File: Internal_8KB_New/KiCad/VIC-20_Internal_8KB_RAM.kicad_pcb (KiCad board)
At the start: 2 copper layers, 66 x 62.2 mm, 11 parts, among them J1 RAM Decoder, J2 UD4, J3 UE4, U1 74HCT04, U2 74HCT138, U3 62256, U4 74HCT30

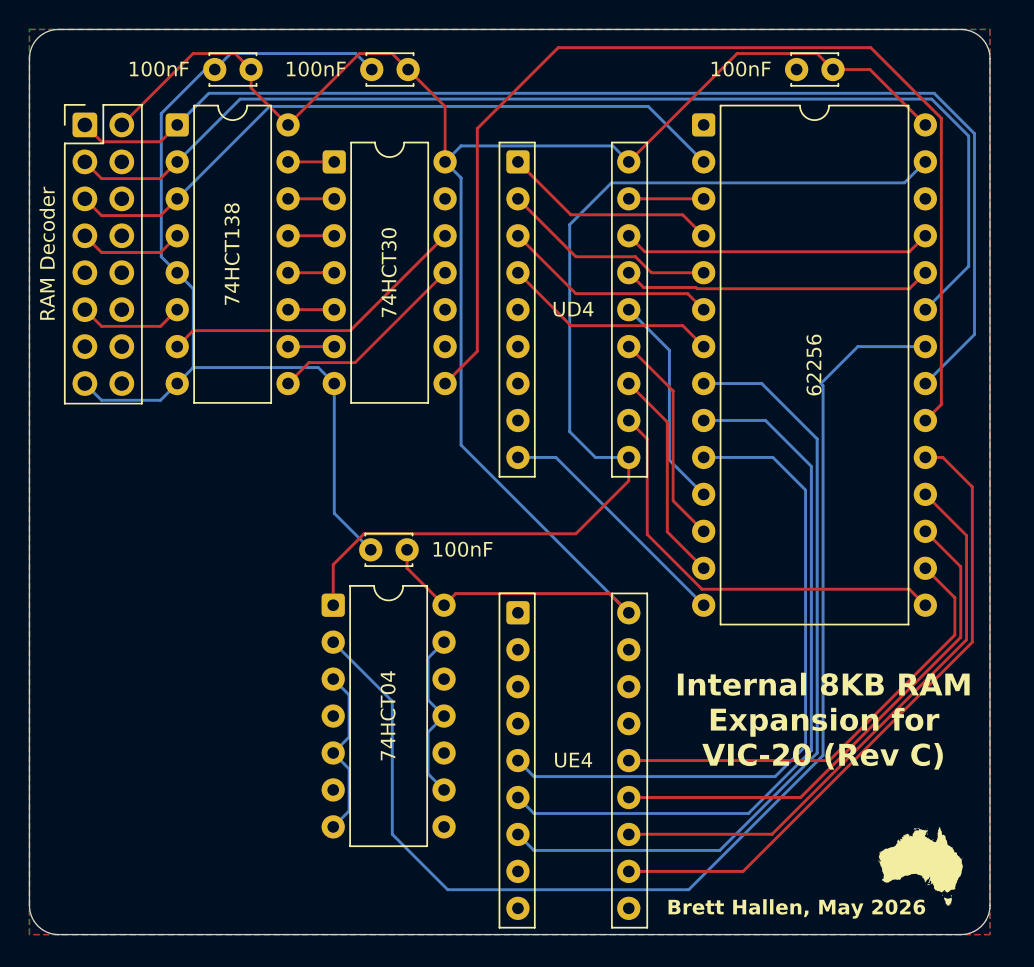
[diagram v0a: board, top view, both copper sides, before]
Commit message: Swapped 62256 -> 6264
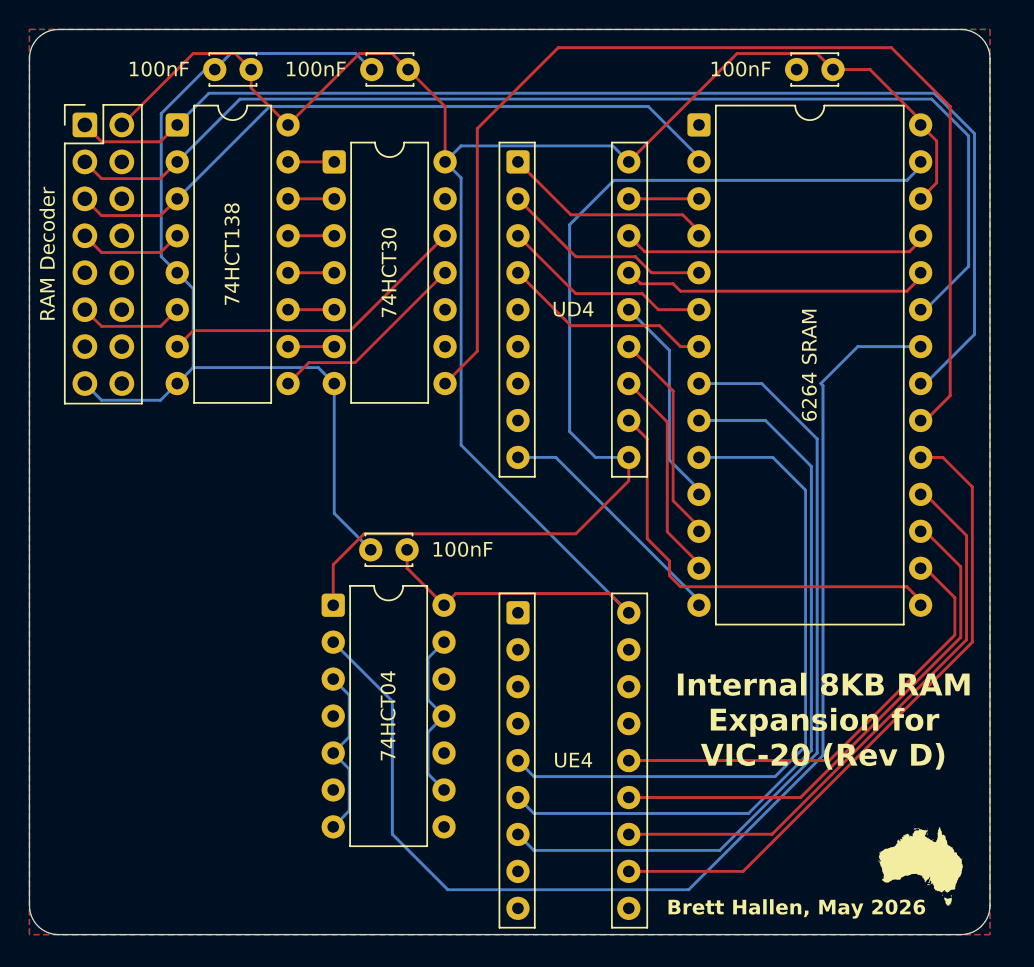
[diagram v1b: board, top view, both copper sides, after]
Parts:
- U3: value 62256 -> 6264 SRAM
- moved U3 0.32 mm to (112.6, 38.1)
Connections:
- U3 pad 26: unconnected-(U3-A13-Pad26) -> +5V
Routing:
- net +5V: track 128.1 -> 134.1 mm
- net /~{RAM_CS}: track 75.9 -> 77.2 mm
- net /BD3: track 29.5 -> 30.3 mm
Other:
- board text added: "27-MAY-2026: Pending testing"
- board text added: "Internal 8KB RAM Expansion for VIC-20 (Rev D)"
- board text removed: "26-MAY-2026: Pending testing"
- board text removed: "Internal 8KB RAM Expansion for VIC-20 (Rev C)"

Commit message: Revised BLK0 expansion
Added enable/disable function to return VIC to unexpanded 5KB state
~RAM1/~RAM2/~RAM3 select signals routed back to VIC when disabled
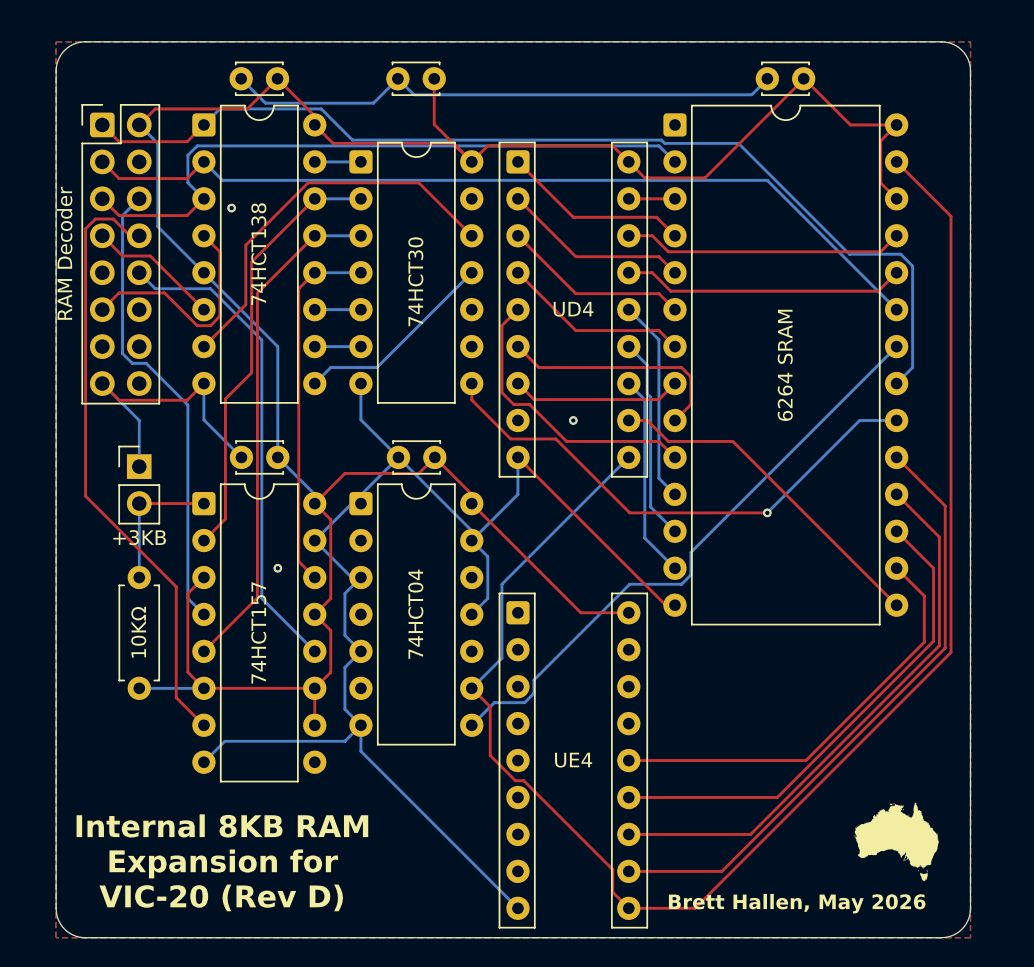
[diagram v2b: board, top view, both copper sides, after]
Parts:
- added C5: 100nF, Capacitor_THT:C_Disc_D3.0mm_W2.0mm_P2.50mm, F.Cu at (119.8, 34.9)
- added J4: +3KB, Connector_PinHeader_2.54mm:PinHeader_1x02_P2.54mm_Vertical, F.Cu at (74.1, 61.6)
- added R1: 10KΩ, Resistor_THT:R_Axial_DIN0207_L6.3mm_D2.5mm_P7.62mm_Horizontal, F.Cu at (74.1, 76.8)
- added U3: 74HCT30, Package_DIP:DIP-14_W7.62mm, F.Cu at (89.3, 40.6)
- U4: value 74HCT30 -> 74HCT157; footprint Package_DIP:DIP-14_W7.62mm -> Package_DIP:DIP-16_W7.62mm
- moved C1 29.5 mm to (94.4, 61.0)
- moved C3 27.4 mm to (94.4, 34.9)
- moved U4 25.1 mm to (78.5, 64.1)
- moved C4 10.9 mm to (83.6, 61.0)
- moved C2 9.00 mm to (83.6, 34.9)
- moved U1 7.24 mm to (89.3, 64.1)
- moved U2 1.83 mm to (78.5, 38.1)
- moved U5 1.65 mm to (110.9, 38.1)
- moved J1 1.20 mm to (71.6, 38.1)
- renumbered U3 to U5
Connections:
- J1 pad 12: unconnected-(J1-Pin_12-Pad12) -> /~{RAM3_{OUT}}
- J1 pad 13: unconnected-(J1-Pin_13-Pad13) -> /~{RAM2_{OUT}}
- J1 pad 14: unconnected-(J1-Pin_14-Pad14) -> /~{RAM1_{OUT}}
- J2 pad 5: unconnected-(J2-Pin_5-Pad5) -> /VA0
- J2 pad 6: unconnected-(J2-Pin_6-Pad6) -> /VA1
- J2 pad 7: unconnected-(J2-Pin_7-Pad7) -> /VA2
- J3 pad 10: unconnected-(J3-Pin_10-Pad10) -> /VR/~{W}
- J3 pad 5: /VA0 -> unconnected-(J3-Pin_5-Pad5)
- J3 pad 6: /VA1 -> unconnected-(J3-Pin_6-Pad6)
- J3 pad 7: /VA2 -> unconnected-(J3-Pin_7-Pad7)
- U1 pad 1: /VR/~{W} -> GND
- U1 pad 2: /~{OE} -> unconnected-(U1-Pad2)
- U1 pad 8: unconnected-(U1-Pad8) -> /~{OE}
- U1 pad 9: GND -> /VR/~{W}
- U2 pad 4: /~{BLK0}/~{G2A} -> /VA13/G1
- U2 pad 5: GND -> +5V
- U2 pad 6: /VA13/G1 -> /~{BLK0}/~{G2A}
- U4 pad 1: /~{RAM0} -> Net-(J4-Pin_2)
- U4 pad 10: (no net) -> +5V
- U4 pad 11: /~{RAM6} -> +5V
- U4 pad 12: /~{RAM7} -> /~{RAM3_{OUT}}
- U4 pad 13: (no net) -> +5V
- U4 pad 14: +5V -> /~{RAM3}
- U4 pad 3: /~{RAM2} -> +5V
- U4 pad 4: /~{RAM3} -> /~{RAM1_{OUT}}
- U4 pad 5: /~{RAM4} -> /~{RAM2}
- U4 pad 6: /~{RAM5} -> +5V
- U4 pad 7: GND -> /~{RAM2_{OUT}}
- U4 pad 8: /~{RAM_CS} -> GND
- U4 pad 9: (no net) -> unconnected-(U4-Zc-Pad9)
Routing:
- net GND: track 107.4 -> 154.9 mm, vias 0 -> 3
- net /VA2: track 54.8 -> 11.7 mm
- net /~{OE}: track 83.8 -> 41.4 mm
- net /~{RAM2_{OUT}}: track 0.00 -> 41.9 mm
- net /~{RAM_CS}: track 77.2 -> 36.2 mm, vias 0 -> 1
- net +5V: track 134.1 -> 171.4 mm
- net /VA1: track 50.7 -> 16.2 mm
- net /~{RAM3_{OUT}}: track 0.00 -> 33.3 mm
- net /VR/~{W}: track 72.4 -> 105.0 mm
- net /~{RAM1_{OUT}}: track 0.00 -> 31.9 mm
- net /~{RAM2}: track 3.18 -> 34.9 mm
- net /VA0: track 46.6 -> 19.9 mm
- net /~{RAM1}: track 3.18 -> 29.8 mm
- net /~{RAM3}: track 3.18 -> 25.0 mm
- net /VA11: track 77.7 -> 59.8 mm
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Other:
- board size 66 x 62.2 mm -> 62.9 x 61.6 mm
- board text added: "28-MAY-2026: Pending testing"
- board text removed: "27-MAY-2026: Pending testing"
- board text removed: "3-to-8 Decoder"
- board text removed: "32KB SRAM"
- board text removed: "8-Input NAND Gate"
- board text removed: "Hex Inverter"
- board text removed: "To/From VIC"
